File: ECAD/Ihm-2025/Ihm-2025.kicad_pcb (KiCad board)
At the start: 2 copper layers, 58 x 58 mm, 23 parts, among them SW1 SW_SPDT, SW2 SW_SPDT, SW3 SW_SPDT, SW4 SW_SPDT

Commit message: New IHM
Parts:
- removed D3, D4, D5: WS2812B, LED_SMD:LED_WS2812B_PLCC4_5.0x5.0mm_P3.2mm
- removed H1: M3, MountingHole:MountingHole_3.2mm_M3_Pad_Via
- removed SW3: SW_SPDT, footprints:SK-12D10 1P2T
- removed kibuzzard-64A1DFBF: G***, kibuzzard-64A1DFBF
- removed kibuzzard-64A1DFD1: G***, kibuzzard-64A1DFD1
- added C2: 100n, Capacitor_SMD:C_1206_3216Metric, B.Cu at (148.6, 97.2)
- added G***: LOGO, LOGO, B.Cu at (155.4, 107.2)
- added H2: M3, MountingHole:MountingHole_3.2mm_M3_Pad_Via, F.Cu at (173.8, 89.5)
- added R1: R_Small, Resistor_SMD:R_1206_3216Metric_Pad1.30x1.75mm_HandSolder, F.Cu at (160.7, 88.9)
- added R2: 4.8k, Resistor_SMD:R_1206_3216Metric_Pad1.30x1.75mm_HandSolder, B.Cu at (152.4, 100.3)
- added U1: ~, Package_TO_SOT_SMD:SOT-23W, B.Cu at (148.8, 101.0)
- added kibuzzard-666F551A: G***, kibuzzard-666F551A, F.Cu at (164.9, 86.4)
- SW1: value SW_SPDT -> SW_Push; footprint footprints:SK-12D10 1P2T -> PCM_Switch_Keyboard_Cherry_MX:SW_Cherry_MX_PCB_1.00u
- moved H3 52.1 mm to (123.8, 89.5)
- moved H4 40.7 mm to (173.8, 112.0)
- moved SW1 34.2 mm to (168.8, 78.1)
- moved G*** 28.0 mm to (140.3, 107.3), turned to 0 degrees
- moved kibuzzard-64A1DFA1 24.7 mm to (137.5, 82.5), turned to 90 degrees
- moved D2 14.9 mm to (156.7, 74.5), turned to -90 degrees
- moved SW4 14.7 mm to (144.8, 82.5), turned to 0 degrees
- moved RV1 10.4 mm to (130.4, 84.5), turned to 90 degrees
- moved C1 6.30 mm to (156.7, 82.4), turned to 180 degrees
- moved D1 5.89 mm to (156.7, 82.4), turned to -90 degrees
- moved kibuzzard-64A1DFD6 5.67 mm to (137.5, 74.5), turned to 90 degrees
- moved G*** 5.32 mm to (162.5, 101.0)
- moved IHM-IO1 5.26 mm to (166.8, 95.9)
- moved kibuzzard-64A1DF73 5.16 mm to (160.6, 106.0)
- moved kibuzzard-64A1DF46 5.13 mm to (160.8, 95.9)
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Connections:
- net DAC0 renamed Analog0
- net DAC1 renamed Analog1
- D1 pad 4: NEO_PIXEL -> Net-(D1-DIN)
- D2 pad 2: Net-(D2-DOUT) -> unconnected-(D2-DOUT-Pad2)
- IHM-IO1 pad 5: Detection -> Tirette
- IHM-IO1 pad 7: IHM_3 -> Init
- SW1 pad 1: GND -> Init
- SW1 pad 2: IHM_3 -> GND
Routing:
- net IHM_3: track 59.9 -> 0.00 mm
- net Detection: track 47.0 -> 0.00 mm
- net +5V: track 63.2 -> 32.4 mm, vias 0 -> 1
- net Tirette: track 0.00 -> 28.7 mm
- net Init: track 0.00 -> 23.7 mm
- net Analog0: track 70.2 -> 48.3 mm
- net IHM_4: track 59.9 -> 50.7 mm, vias 0 -> 1
- net GND: track 0.00 -> 7.86 mm, vias 3 -> 4
- net NEO_PIXEL: track 15.4 -> 8.87 mm
- net +3V3: track 61.4 -> 66.7 mm
- net Net-(D4-DOUT): track 4.58 -> 0.00 mm
- net Net-(D3-DOUT): track 4.58 -> 0.00 mm
- net Net-(D2-DOUT): track 4.58 -> 0.00 mm
- net Net-(D1-DIN): track 0.00 -> 4.44 mm
- net Couleur: track 30.8 -> 34.0 mm
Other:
- board size 58 x 58 mm -> 58 x 46 mm
- board text added: "Karibous 2024-25"
- board text removed: "Karibous 2023-24"

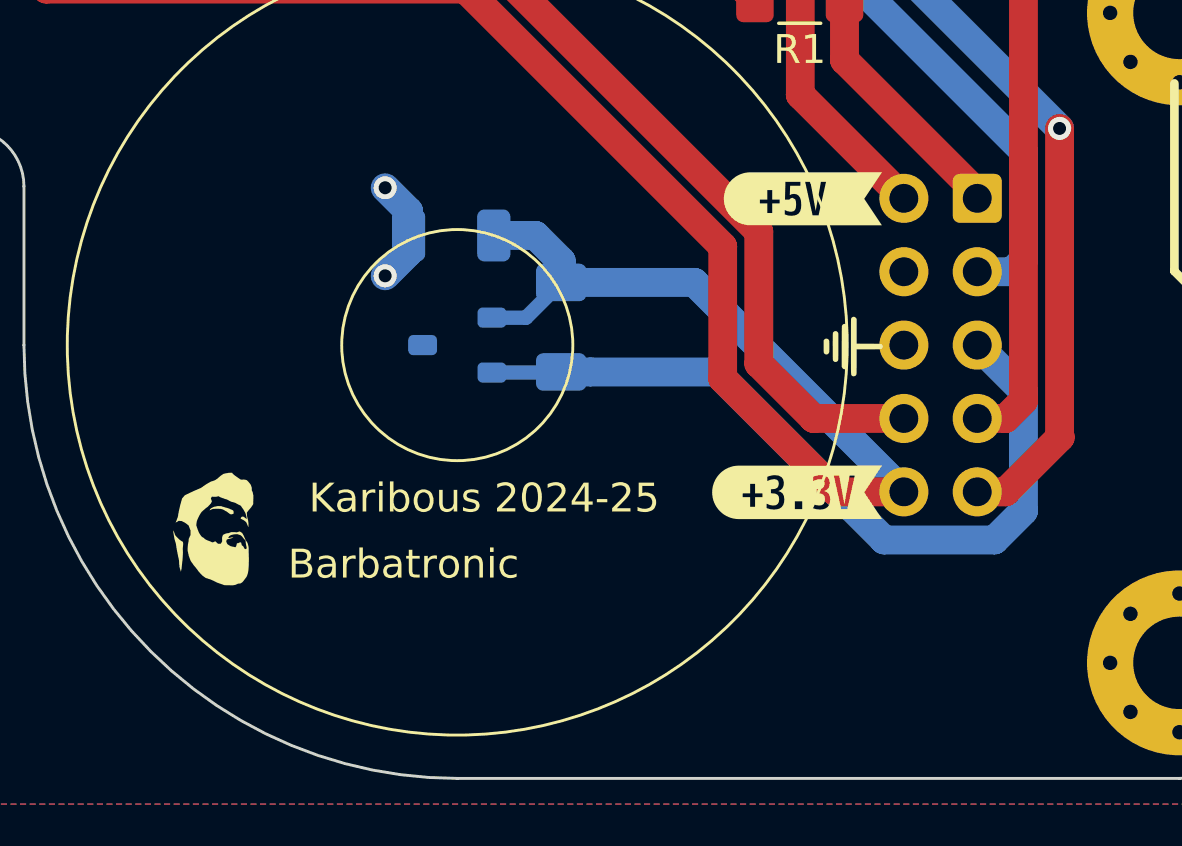
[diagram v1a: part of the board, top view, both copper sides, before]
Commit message: New halle effect sensor for tirette
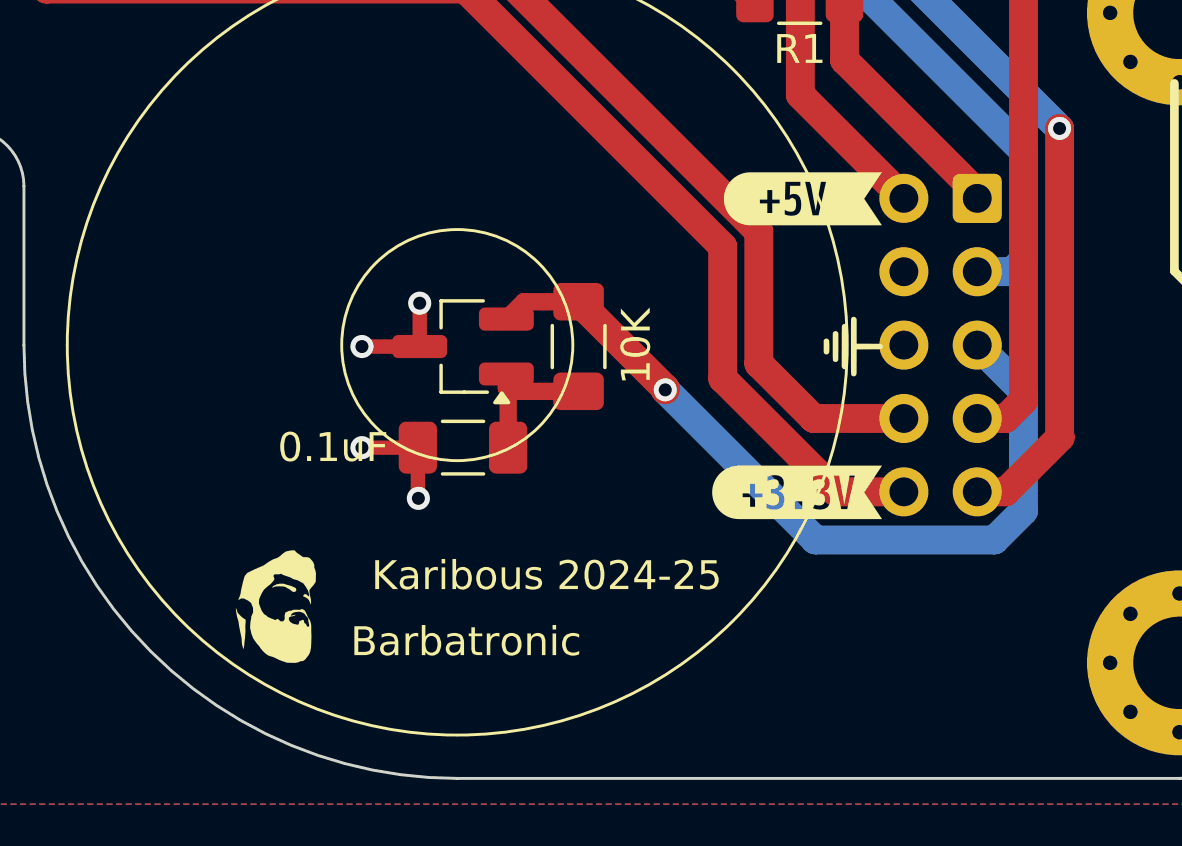
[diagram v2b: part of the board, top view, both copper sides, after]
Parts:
- removed C2: 100n, Capacitor_SMD:C_1206_3216Metric
- removed R2: 4.8k, Resistor_SMD:R_1206_3216Metric_Pad1.30x1.75mm_HandSolder
- removed U1: ~, Package_TO_SOT_SMD:SOT-23W
- added C3: 0.1uF, Capacitor_SMD:C_1206_3216Metric_Pad1.33x1.80mm_HandSolder, F.Cu at (149.0, 104.5)
- added R3: 10K, Resistor_SMD:R_1206_3216Metric_Pad1.30x1.75mm_HandSolder, F.Cu at (153.0, 101.0)
- added U2: DRV5023, Package_TO_SOT_SMD:SOT-23_Handsoldering, F.Cu at (149.0, 101.0)
- moved G*** 3.45 mm to (142.5, 110.0)
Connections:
- net IHM_4 renamed Detection
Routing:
- net +3V3: track 66.7 -> 45.5 mm
- net +3.3V: track 0.00 -> 5.61 mm
- net GND: track 7.86 -> 11.3 mm, vias 4 -> 6
- net Tirette: track 28.7 -> 28.4 mm, vias 0 -> 1

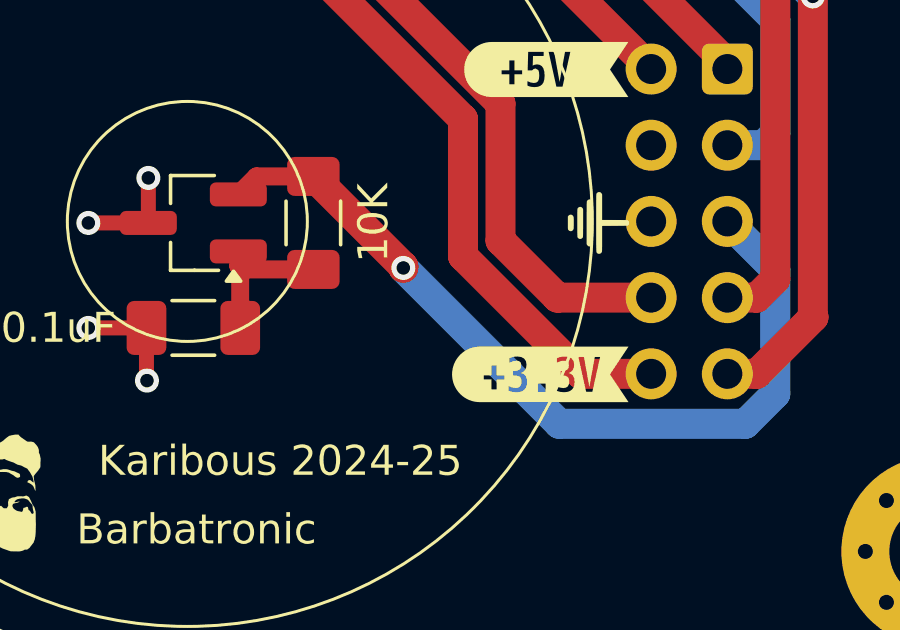
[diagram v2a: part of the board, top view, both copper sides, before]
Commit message: fix 3.3V not connected to tirette
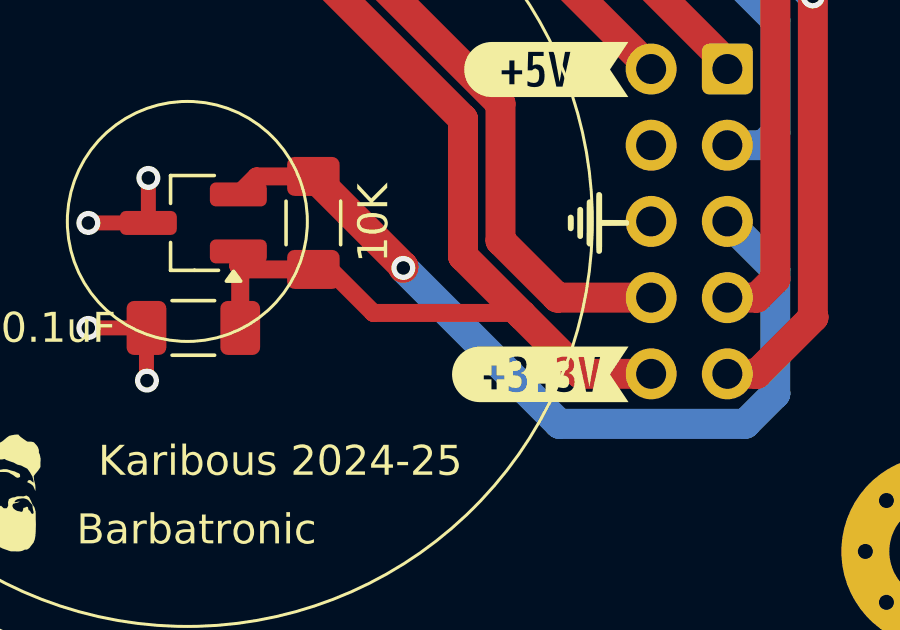
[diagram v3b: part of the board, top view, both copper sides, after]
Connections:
- C3 pad 1: +3.3V -> +3V3
- R3 pad 2: +3.3V -> +3V3
- U2 pad 1: +3.3V -> +3V3
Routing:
- net +3V3: track 45.5 -> 58.7 mm
- net +3.3V: track 5.61 -> 0.00 mm
